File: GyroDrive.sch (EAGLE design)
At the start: 42 parts, among them IC1 AD8235, IC2 AD8235, IC3 AD8235, IC4 AD8235

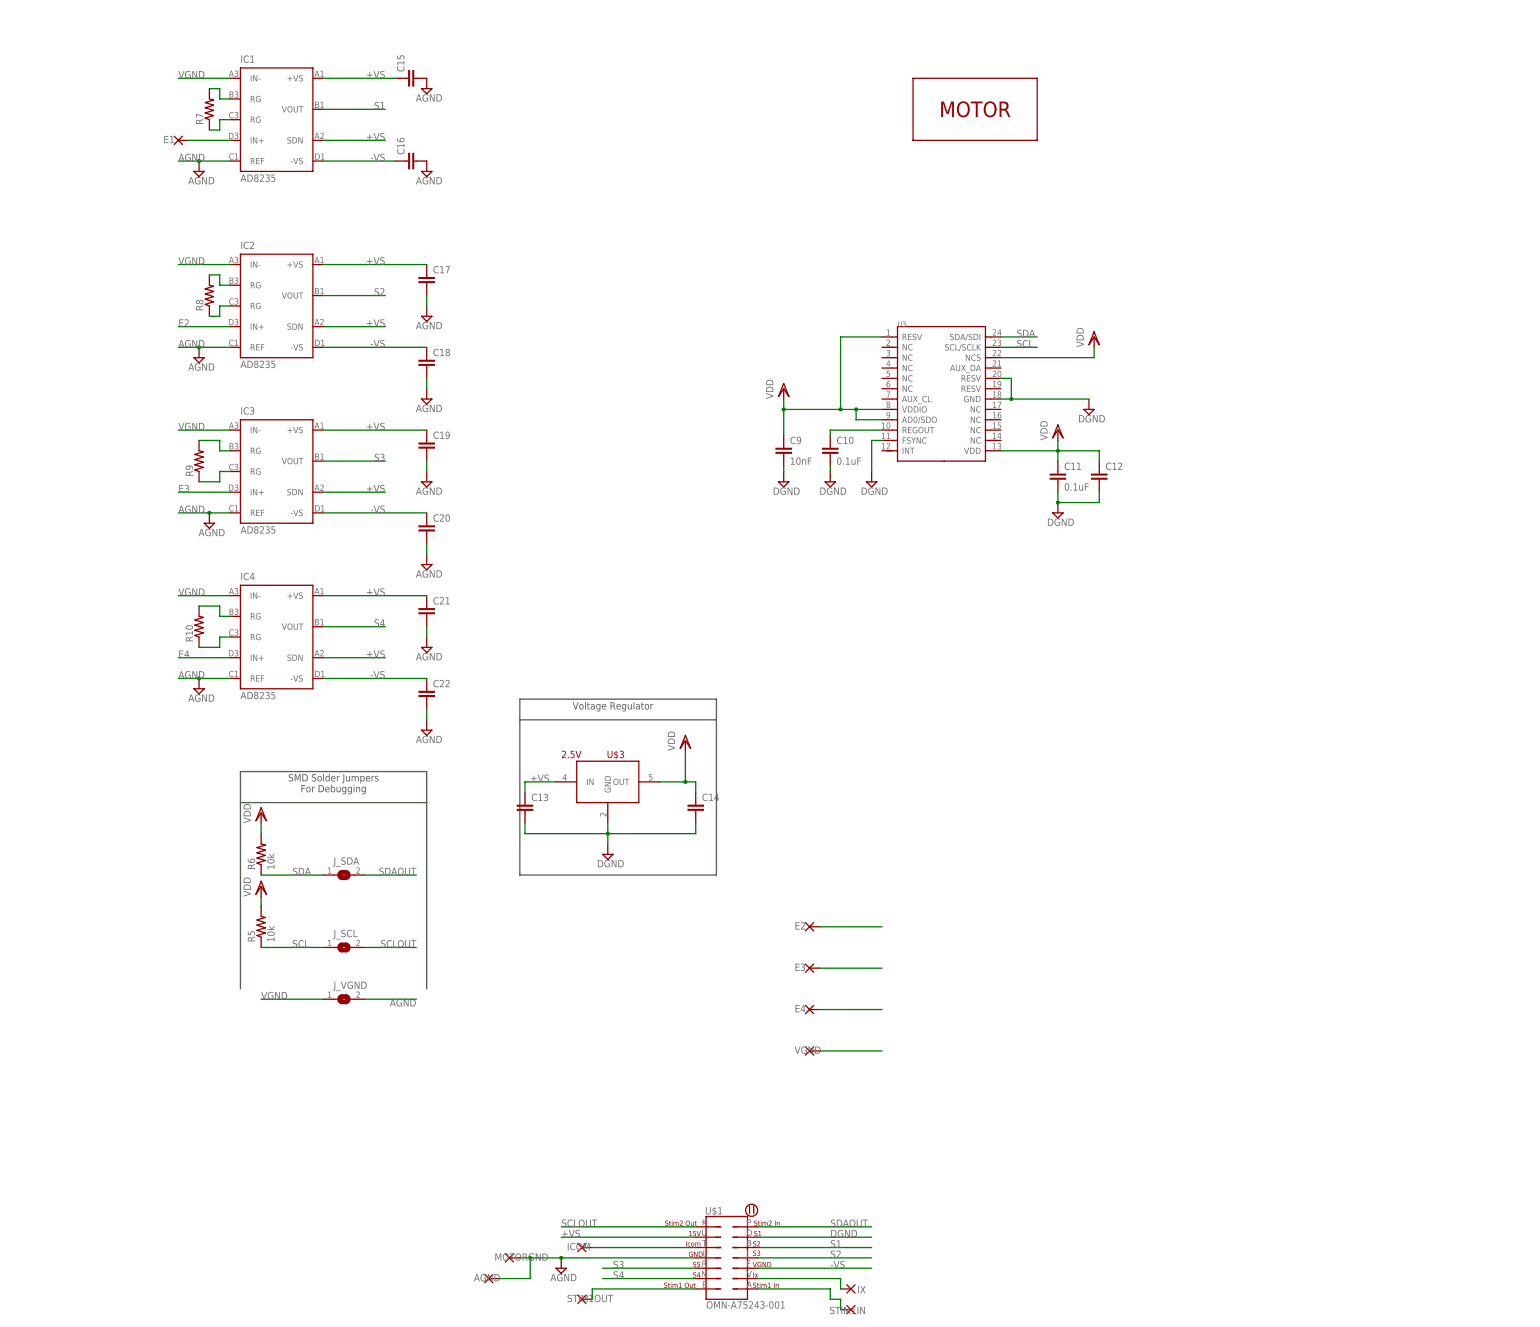
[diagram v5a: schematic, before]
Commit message: Changed pinout, spaced vias for in-amps to minimum distance that avoids errors
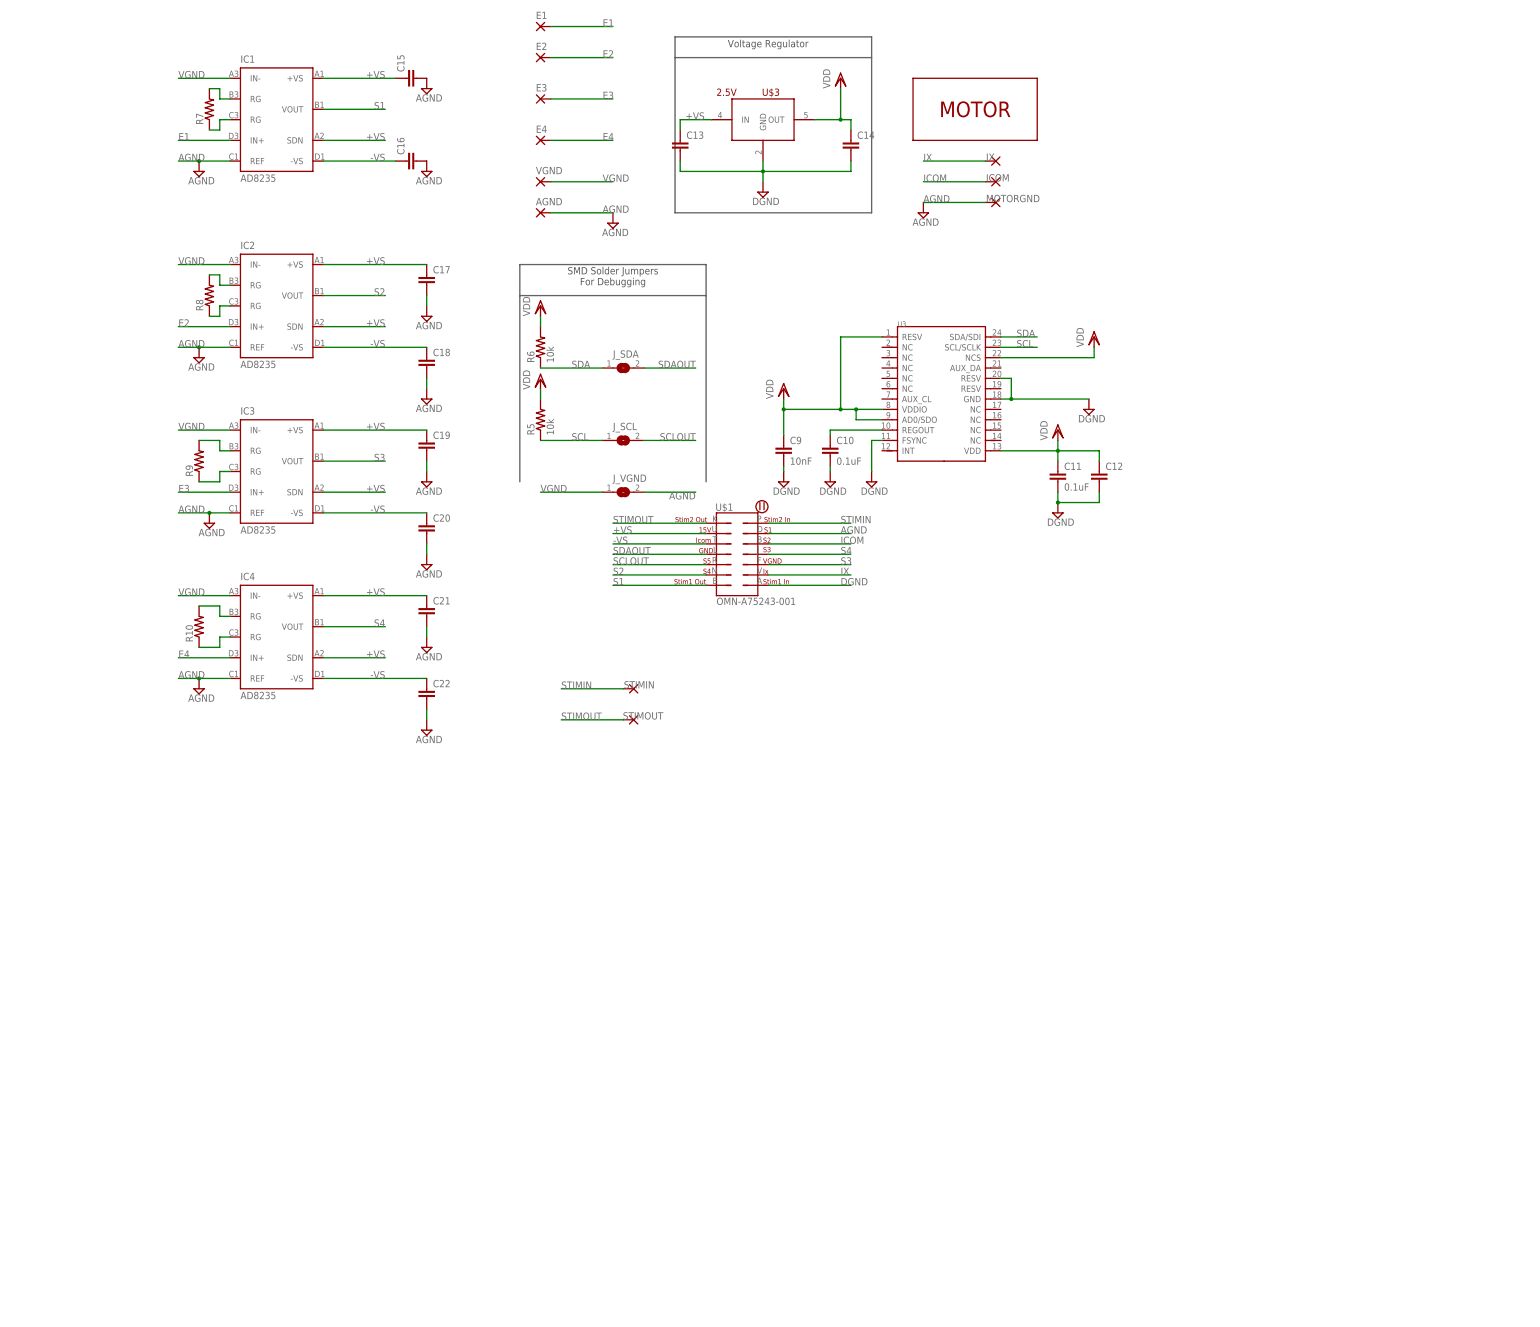
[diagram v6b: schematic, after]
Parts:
- removed STIM1IN, STIM1OUT: (no value), michael-stetner:THROUGH-HOLE-30MIL/15MIL
- added STIMIN, STIMOUT: (no value), michael-stetner:THROUGH-HOLE-30MIL/15MIL
- AGND, E1, E2, E3, E4, VGND: device michael-stetner:THROUGH-HOLE-30MIL/15MIL -> michael-stetner:SMD25-25-MIL
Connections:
- net N$14 renamed IX
- removed net N$15: STIM1IN.P, U$1.A
- removed net N$16: STIM1OUT.P, U$1.E
- removed net N$17: ICOM.P, U$1.T
- new net ICOM: ICOM.P, U$1.B
- new net STIMIN: STIMIN.P, U$1.P
- new net STIMOUT: STIMOUT.P, U$1.K
- net -VS: now also U$1.T; no longer U$1.F
- net AGND: now also U$1.D; no longer U$1.L
- net DGND: now also U$1.A; no longer U$1.D
- net S1: now also U$1.E; no longer U$1.B
- net S2: now also U$1.N; no longer U$1.J
- net S3: now also U$1.F; no longer U$1.R
- net S4: now also U$1.J; no longer U$1.N
- net SCLOUT: now also U$1.R; no longer U$1.K
- net SDAOUT: now also U$1.L; no longer U$1.P
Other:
- moved on the sheet: C13, C14, ICOM, IX, J_SCL, J_SDA, J_VGND, MOTORGND, R5, R6, U$1, U$3

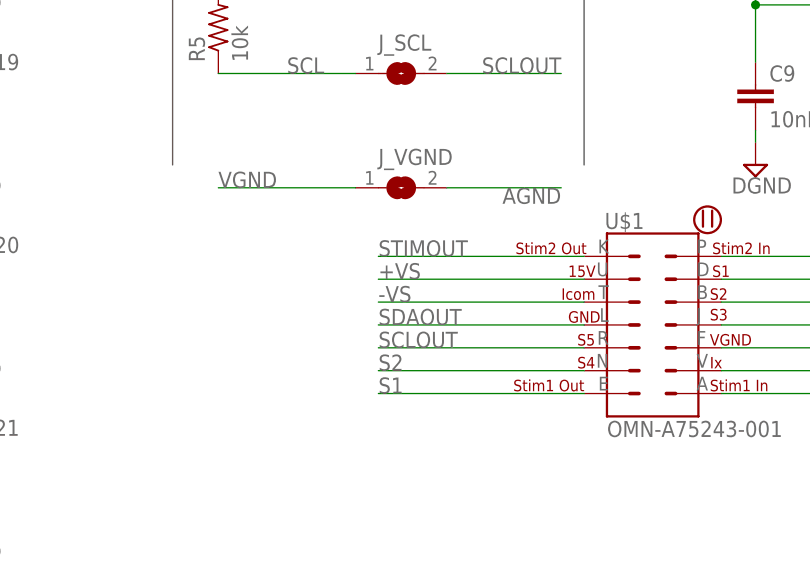
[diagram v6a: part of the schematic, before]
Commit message: Switched +VS and -VS on pinout and analog power layer. Finished routing!
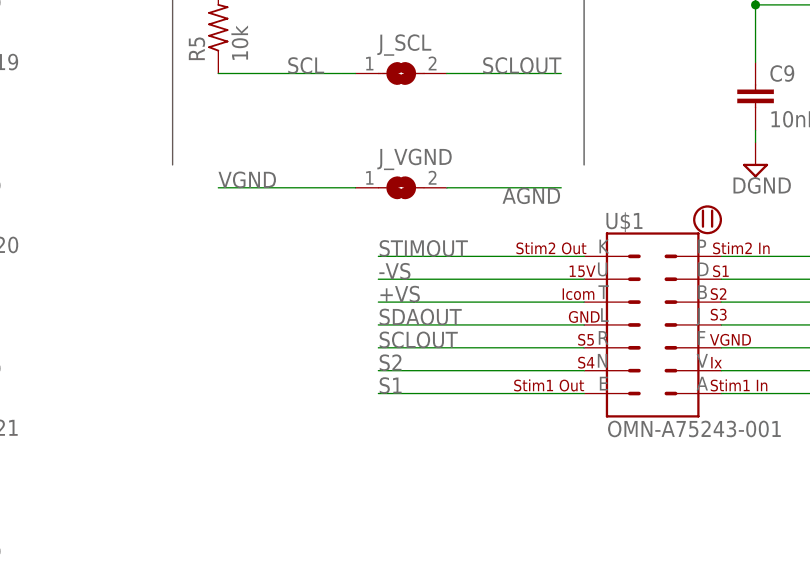
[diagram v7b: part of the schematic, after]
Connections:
- net +VS: now also U$1.T; no longer U$1.U
- net -VS: now also U$1.U; no longer U$1.T
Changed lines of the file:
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@@
 </segment>
-<segment>
-<pinref part="U$1" gate="G$1" pin="T"/>
-<wire x1="137.16" y1="50.8" x2="114.3" y2="50.8" width="0.1524" layer="91"/>
-<label x="114.3" y="50.8" size="1.778" layer="95"/>
-</segment>
-</net>
-<net name="+VS" class="0">
 <segment>
 <pinref part="U$1" gate="G$1" pin="U"/>
@@
 <label x="114.3" y="53.34" size="1.778" layer="95"/>
 </segment>
+</net>
+<net name="+VS" class="0">
 <segment>
 <pinref part="U$3" gate="G$1" pin="IN"/>
@@
 <label x="58.42" y="22.86" size="1.778" layer="95" rot="MR0"/>
 </segment>
+<segment>
+<pinref part="U$1" gate="G$1" pin="T"/>
+<wire x1="137.16" y1="50.8" x2="114.3" y2="50.8" width="0.1524" layer="91"/>
+<label x="114.3" y="50.8" size="1.778" layer="95"/>
+</segment>
 </net>

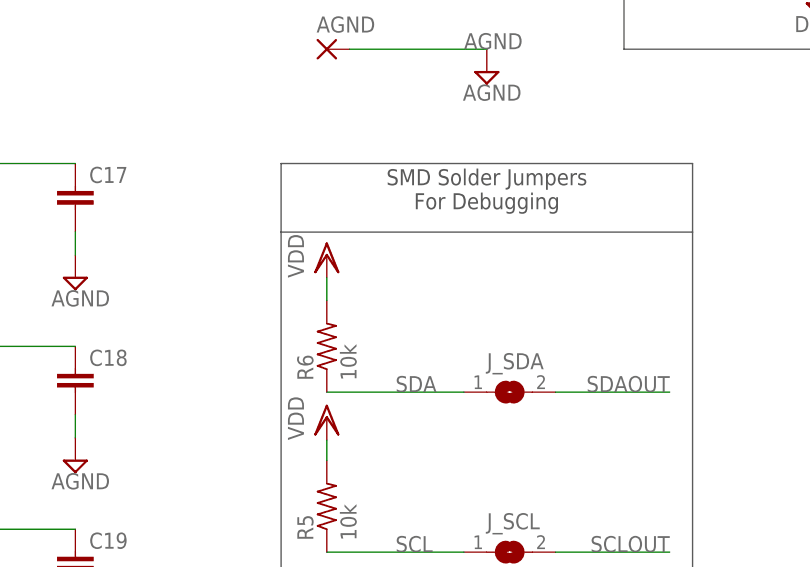
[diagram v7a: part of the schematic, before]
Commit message: Added bypass capacitor for SDA pull-up resistor, shorted SDA and SCL jumpers with traces
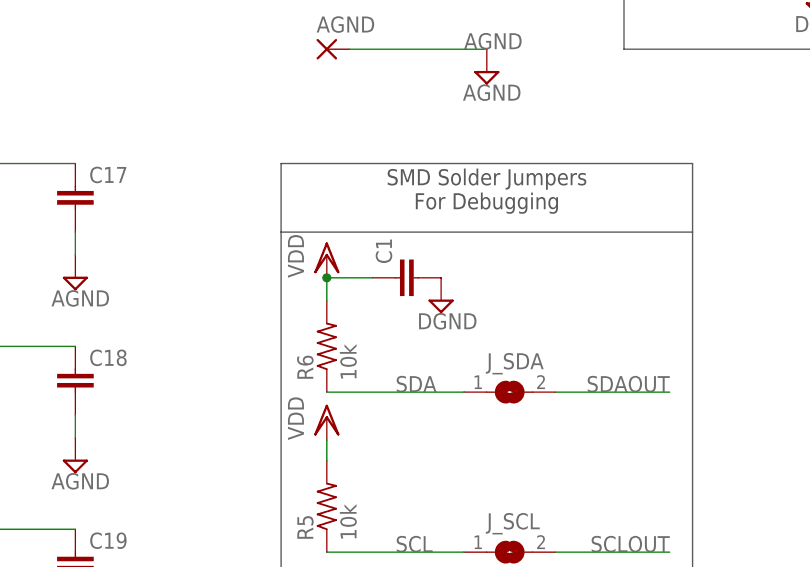
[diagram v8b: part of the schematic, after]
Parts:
- added C1: (no value), resistor:C-EUC0201
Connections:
- net DGND: now also C1.2
- net VDD: now also C1.1
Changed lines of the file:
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@@
 <part name="AGND" library="michael-stetner" deviceset="SMD25-25-MIL" device=""/>
 <part name="E1" library="michael-stetner" deviceset="SMD25-25-MIL" device=""/>
+<part name="C1" library="resistor" deviceset="C-EU" device="C0201"/>
+<part name="SUPPLY3" library="supply2" deviceset="DGND" device=""/>
 </parts>
 <sheets>
@@
 <instance part="AGND" gate="1" x="96.52" y="132.08"/>
 <instance part="E1" gate="1" x="96.52" y="177.8"/>
+<instance part="C1" gate="G$1" x="104.14" y="106.68" rot="R90"/>
+<instance part="SUPPLY3" gate="G$1" x="109.22" y="104.14"/>
 </instances>
 <busses>
@@
 <label x="170.18" y="40.64" size="1.778" layer="95"/>
 </segment>
+<segment>
+<pinref part="C1" gate="G$1" pin="2"/>
+<pinref part="SUPPLY3" gate="G$1" pin="DGND"/>
+</segment>
 </net>
 <net name="SDA" class="0">
@@
 </segment>
 <segment>
-<label x="104.14" y="93.98" size="1.778" layer="95"/>
 <pinref part="J_SDA" gate="1" pin="1"/>
 <pinref part="R6" gate="G$1" pin="1"/>
 <wire x1="111.76" y1="93.98" x2="96.52" y2="93.98" width="0.1524" layer="91"/>
+<label x="104.14" y="93.98" size="1.778" layer="95"/>
 </segment>
 </net>
@@
 <wire x1="96.52" y1="106.68" x2="96.52" y2="104.14" width="0.1524" layer="91"/>
 <pinref part="VDD5" gate="G$1" pin="VDD"/>
-</segment>
-<segment>
+<pinref part="C1" gate="G$1" pin="1"/>
+<wire x1="101.6" y1="106.68" x2="96.52" y2="106.68" width="0.1524" layer="91"/>
+<junction x="96.52" y="106.68"/>
+</segment>
+<segment>
